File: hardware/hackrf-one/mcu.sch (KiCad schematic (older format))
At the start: 117 parts, among them J1 GSG-USB-MICRO-B, P1 1V8, P10 CTOUT_2, P11 CTIN_2, P12 RTC, P13 VBUS, P17 SSP0, P20 GPIO, P21 ANALOG, P22 I2S, P23 DBGEN, P24 TRST, P25 LPC_ISP, P26 LPC_JTAG, P28 SD, P29 CPLD_JTAG, P3 GND, P30 BANK2_AUX, P31 BANK1_AUX, P35 GCK0, P5 WAKEUP, P7 CTIN_4, P8 VCC, P9 CTOUT_4, SW1 DFU, SW2 RESET, U20 W25Q80BV, U21 TPS62410, U22 GSG-IP4220CZ6, U23 LPC43XXFBD144, U24 GSG-XC2C64A-7VQG100C, X2 MCU_XTAL, X3 CRYSTAL

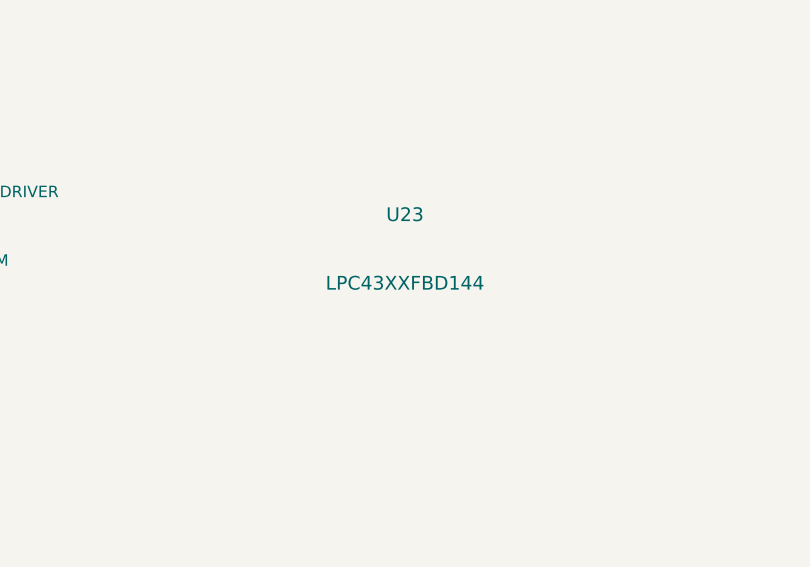
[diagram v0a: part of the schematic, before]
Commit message: change to LPC4320
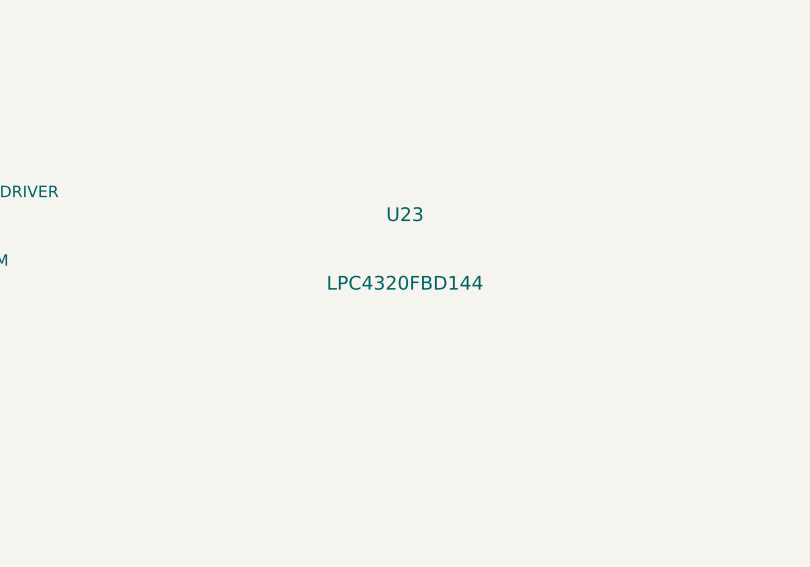
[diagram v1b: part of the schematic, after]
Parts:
- U23: value LPC43XXFBD144 -> LPC4320FBD144; Part Number LPC4330FBD144,551 -> LPC4320FBD144,551
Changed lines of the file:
@@
 P 7000 4750
 F 0 "U23" H 7000 4900 60  0000 C CNN
-F 1 "LPC43XXFBD144" H 7000 4600 60  0000 C CNN
+F 1 "LPC4320FBD144" H 7000 4600 60  0000 C CNN
 F 2 "" H 7000 4750 60  0001 C CNN
 F 3 "" H 7000 4750 60  0001 C CNN
 F 4 "NXP" H 7000 4750 60  0001 C CNN "Manufacturer"
-F 5 "LPC4330FBD144,551" H 7000 4750 60  0001 C CNN "Part Number"
+F 5 "LPC4320FBD144,551" H 7000 4750 60  0001 C CNN "Part Number"
 F 6 "IC MCU 32BIT 144LQFP" H 7000 4750 60  0001 C CNN "Description"
 	1    7000 4750

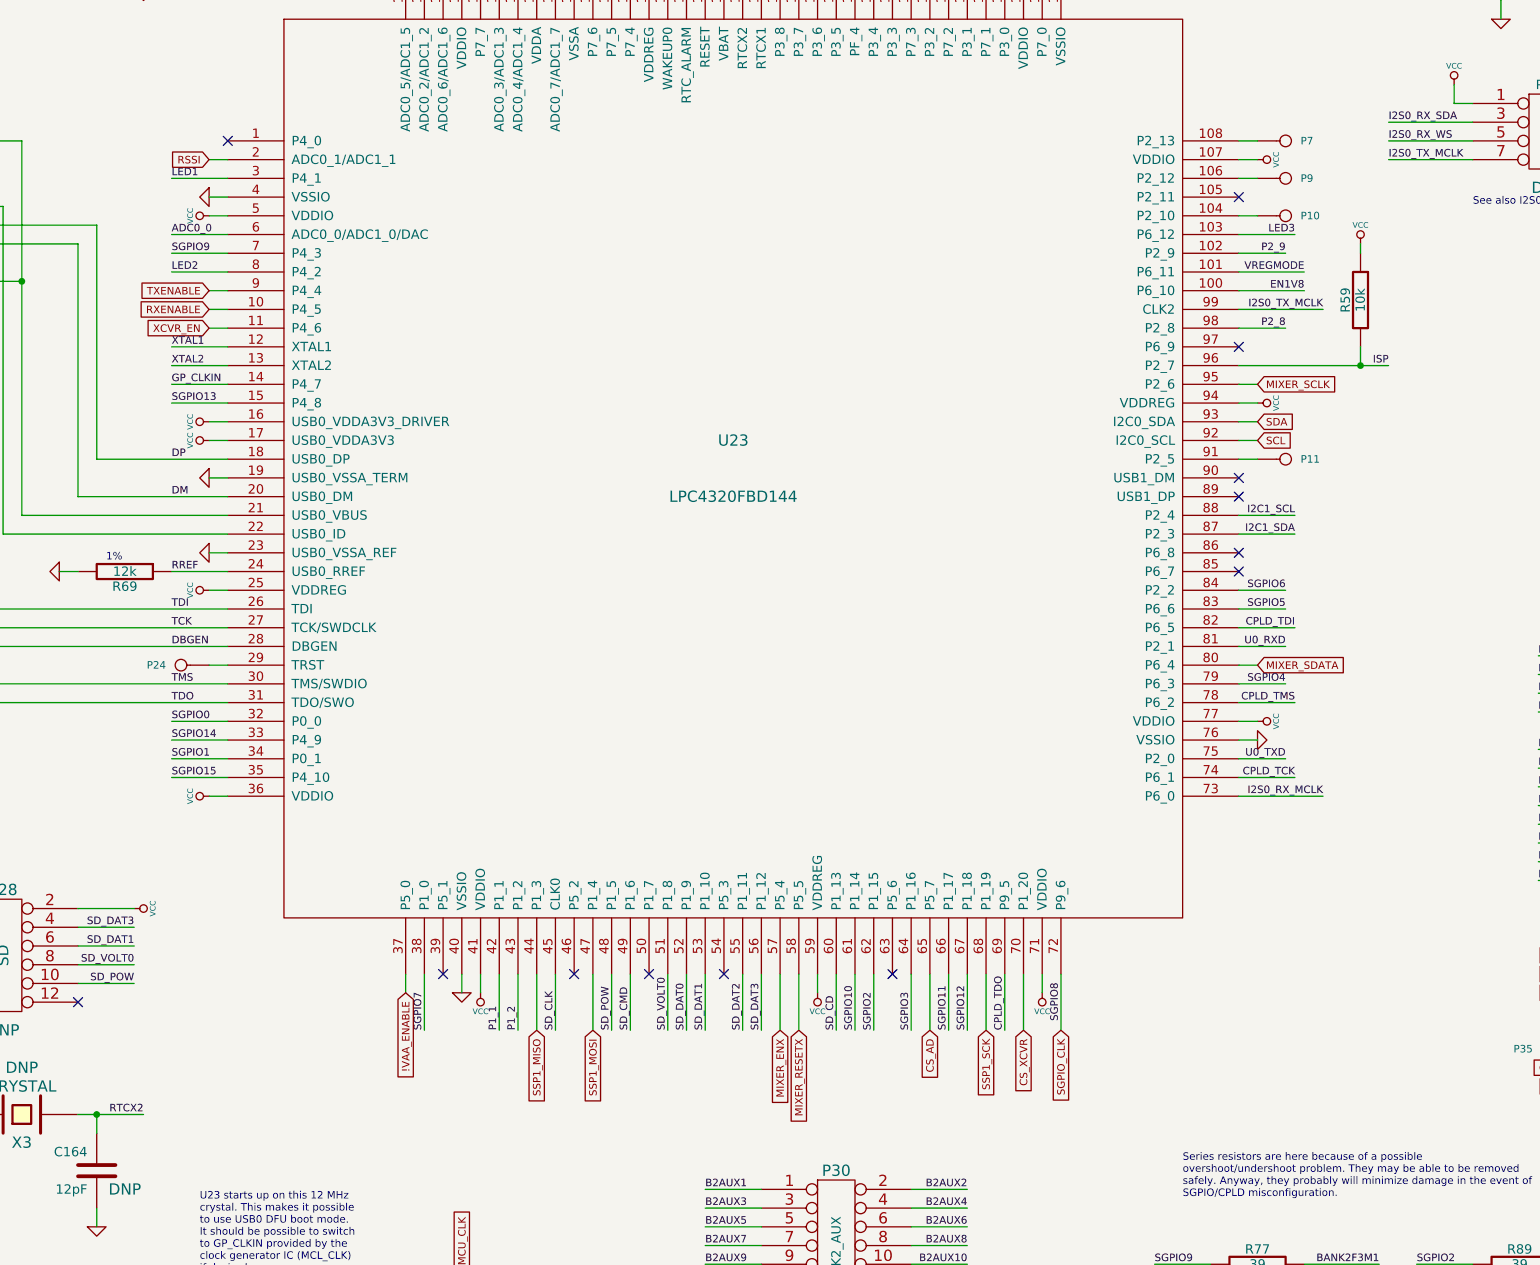
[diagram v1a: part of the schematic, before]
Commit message: removed RF switch logic ICs, replaced with direct GPIO
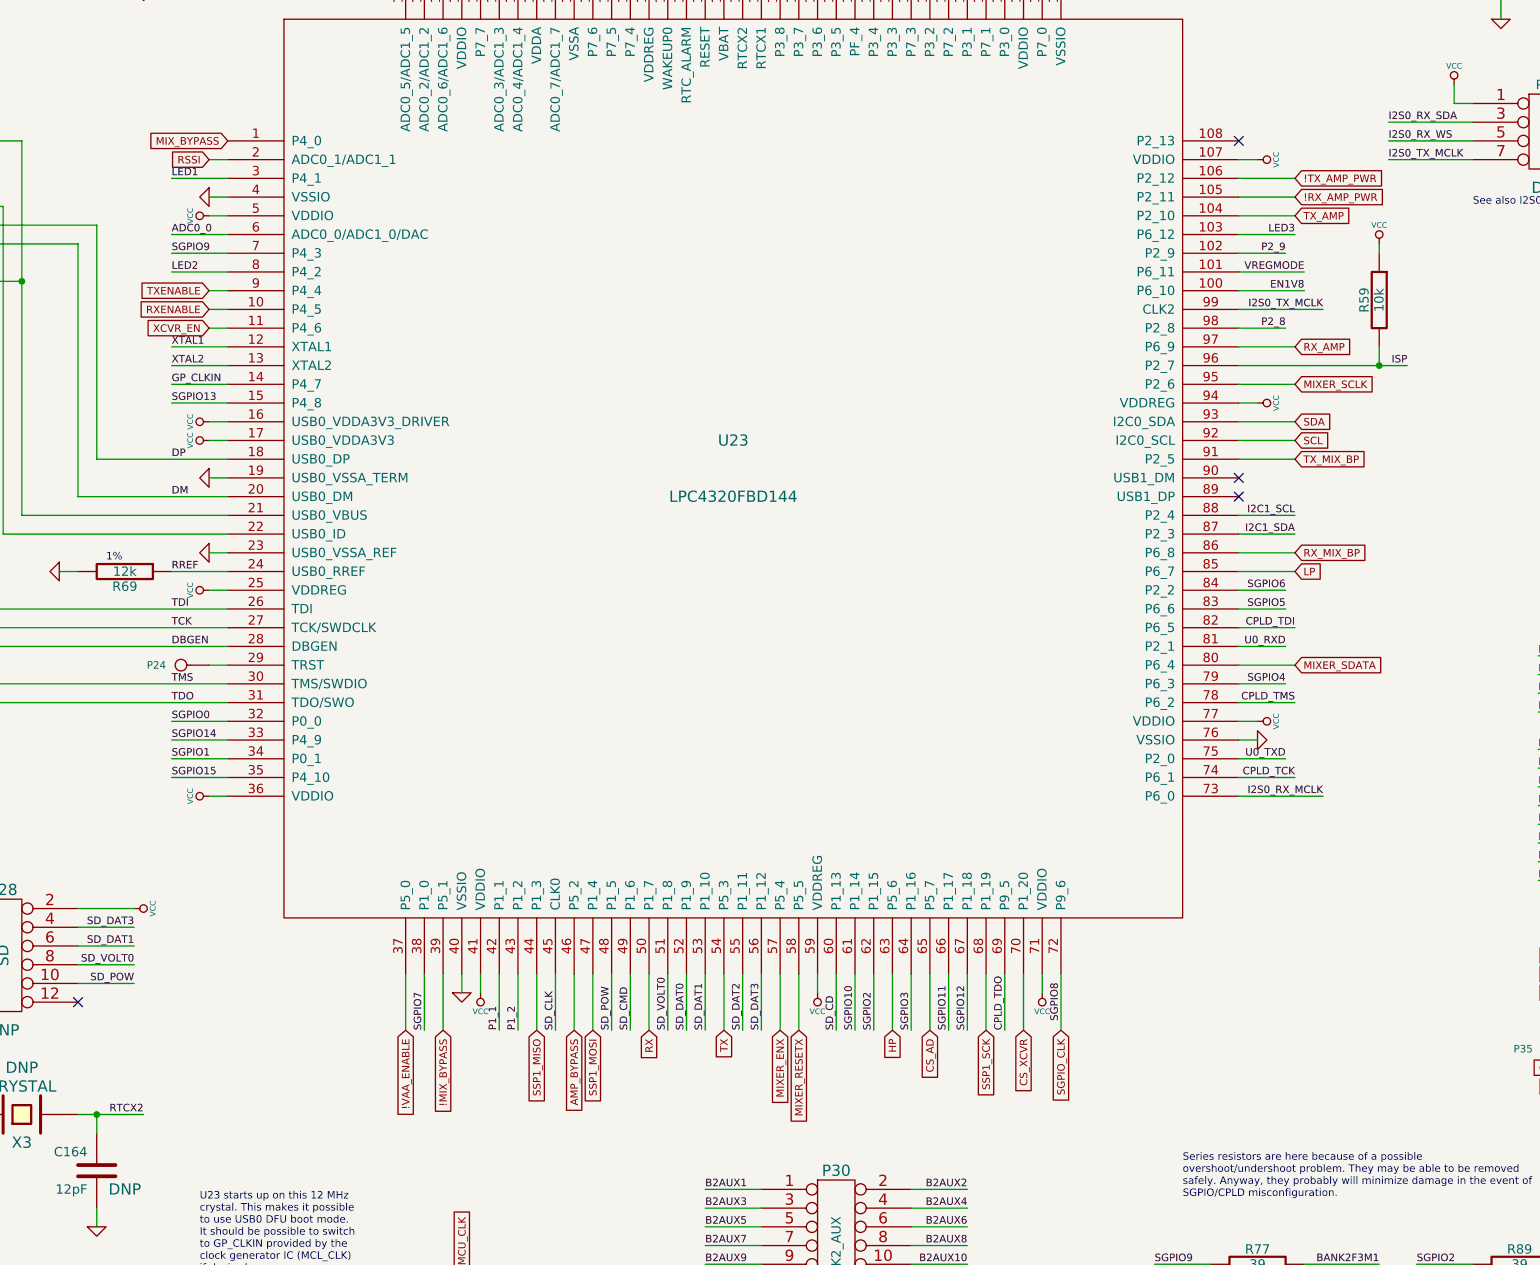
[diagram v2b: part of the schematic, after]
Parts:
- removed P10: CTOUT_2, symbol CONN_1
- removed P11: CTIN_2, symbol CONN_1
- removed P7: CTIN_4, symbol CONN_1
- removed P9: CTOUT_4, symbol CONN_1
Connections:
- net MIX_BYPASS: now reaches U23.1 (P4_0)
- net TX_AMP: now reaches U23.104 (P2_10)
- net !RX_AMP_PWR: now reaches U23.105 (P2_11)
- net !TX_AMP_PWR: now reaches U23.106 (P2_12)
- net !MIX_BYPASS: now reaches U23.39 (P5_1)
- net AMP_BYPASS: now reaches U23.46 (P5_2)
- net RX: now reaches U23.50 (P1_7)
- net TX: now reaches U23.54 (P5_3)
- net HP: now reaches U23.63 (P5_6)
- net LP: now reaches U23.85 (P6_7)
- net RX_MIX_BP: now reaches U23.86 (P6_8)
- net TX_MIX_BP: now reaches U23.91 (P2_5)
- net RX_AMP: now reaches U23.97 (P6_9)
- no-connect marks 23 -> 14
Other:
- moved on the sheet: R59

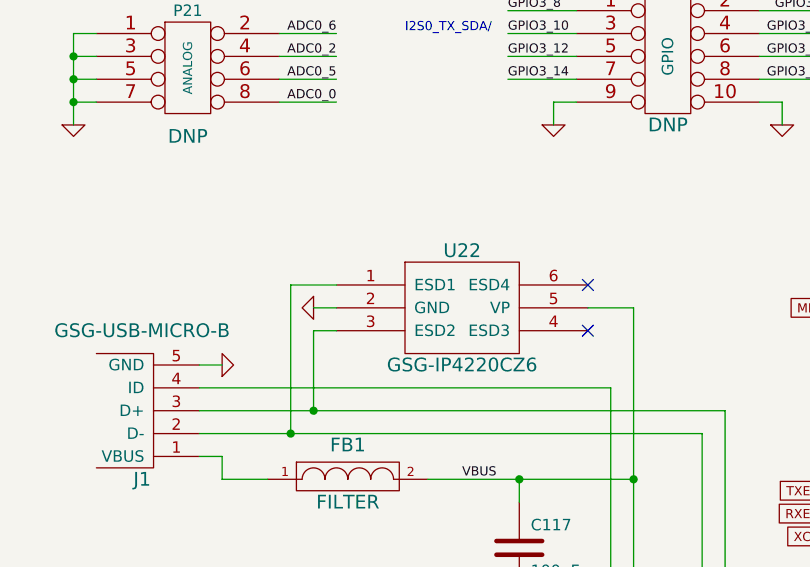
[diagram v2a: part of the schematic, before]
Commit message: USB0_ID pull-up
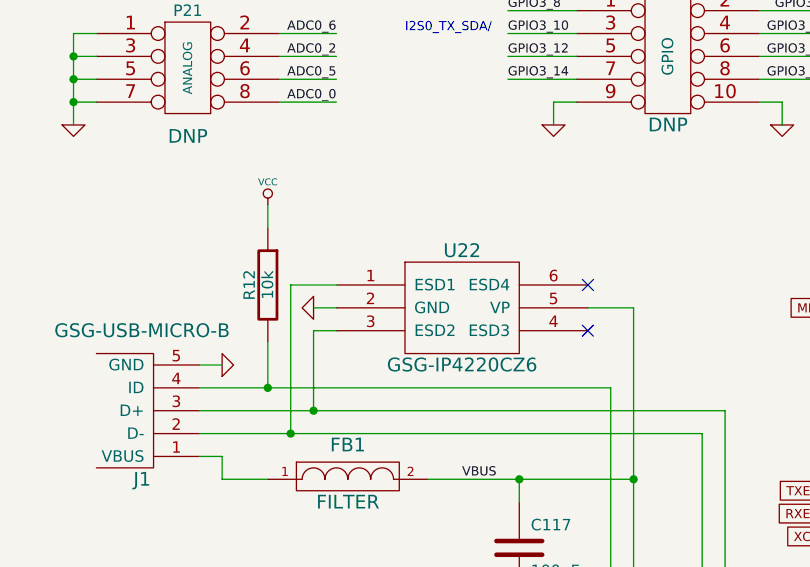
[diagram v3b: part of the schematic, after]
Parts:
- added R12: 10k, symbol R
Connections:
- net VCC: now also R12.1
- net at J1.4 (ID), U23.22 (USB0_ID): now also R12.2

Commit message: module selection update to agree with recent schematic changes
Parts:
- X3: value CRYSTAL -> RTC_XTAL

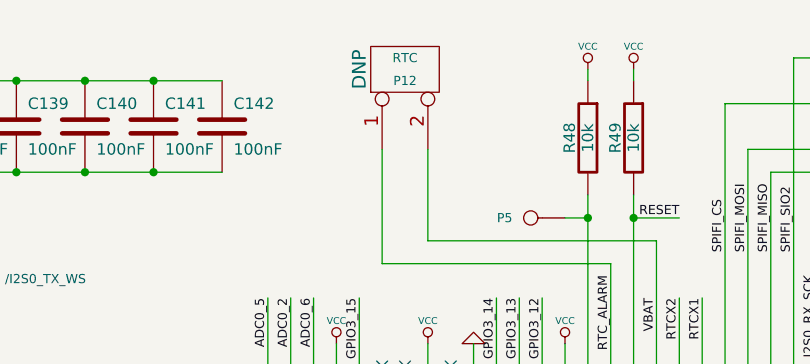
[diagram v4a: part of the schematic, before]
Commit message: analog baseband headers
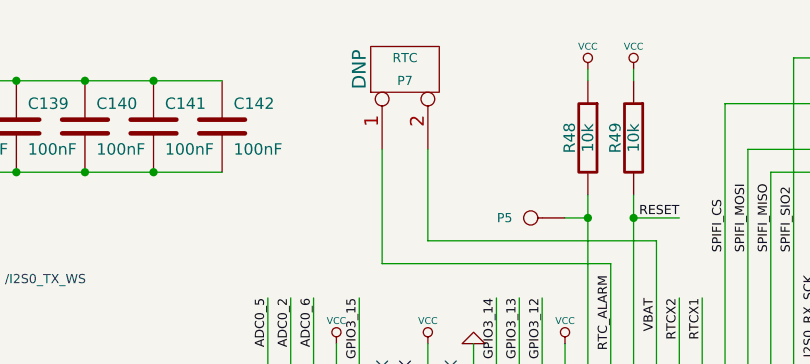
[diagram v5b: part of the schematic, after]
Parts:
- renumbered P12 to P7

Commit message: CPLD layout
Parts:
- removed P35: GCK0, symbol CONN_1
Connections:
- no-connect marks 14 -> 15
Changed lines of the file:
@@
 $EndComp
 $Comp
-L CONN_1 P35
-U 1 1 5047CDF2
-P 11350 7850
-F 0 "P35" H 11430 7850 40  0000 L CNN
-F 1 "GCK0" H 11350 7905 30  0001 C CNN
-F 2 "" H 11350 7850 60  0001 C CNN
-F 3 "" H 11350 7850 60  0001 C CNN
-F 4 "DNP" H 11350 7850 60  0001 C CNN "Note"
-	1    11350 7850
-	-1   0    0    1
-$EndComp
-$Comp
 L R R7
 U 1 1 504786E0
@@
 	1000 9700 800  9700
 Wire Wire Line
-	11500 7850 11600 7850
-Wire Wire Line
 	16150 650  16250 650
 Wire Wire Line
@@
 	1600 3150 1600 3350
 Connection ~ 1600 3350
+NoConn ~ 11600 7850
 $EndSCHEMATC
